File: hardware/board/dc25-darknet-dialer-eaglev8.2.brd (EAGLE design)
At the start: 101.6 x 101.6 mm, 96 parts, among them J1 MF-CON-MICROUSB-RIGHT, SW1 RESET, U1 BU33SD5WG-TR, U2 MCP73831T-5ACI/OT, U3 SOP22FLAT, Y1 CSTCE8M00G52-R0

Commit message: updated schematic to populate audio
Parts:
- C2: value 10uF DNP -> GRM188C80G106ME47D
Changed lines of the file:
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@@
 <attribute name="NAME" x="49.990375" y="32.5755" size="0.6096" layer="26" font="vector" rot="MR180"/>
 </element>
-<element name="C2" library="darknet_parts_library" package="C0603" value="10uF DNP" x="44.846875" y="31.4325" smashed="yes" rot="MR0">
+<element name="C2" library="darknet_parts_library" package="C0603" value="GRM188C80G106ME47D" x="44.846875" y="31.4325" smashed="yes" rot="MR0">
 <attribute name="NAME" x="42.95775" y="31.162625" size="0.6096" layer="26" rot="MR0"/>
 </element>

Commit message: Helps if one saves
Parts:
- R30, R33, R34, R35: value 2K DNP -> 2K
- R31, R32: value 1K DNP -> 1K
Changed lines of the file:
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@@
 </element>
 <element name="U$11" library="darknet_parts_library" package="SPDT_SSAJ120100" value="SWITCH_SPDT" x="50.879375" y="84.93125" rot="MR270"/>
-<element name="R33" library="darknet_parts_library" package="0603-RES" value="2K DNP" x="48.10125" y="35.71875" smashed="yes" rot="MR0">
+<element name="R33" library="darknet_parts_library" package="0603-RES" value="2K" x="48.10125" y="35.71875" smashed="yes" rot="MR0">
 <attribute name="NAME" x="49.990375" y="36.068" size="0.6096" layer="26" font="vector" rot="MR180"/>
 </element>
-<element name="R31" library="darknet_parts_library" package="0603-RES" value="1K DNP" x="44.846875" y="35.71875" smashed="yes" rot="MR180">
+<element name="R31" library="darknet_parts_library" package="0603-RES" value="1K" x="44.846875" y="35.71875" smashed="yes" rot="MR180">
 <attribute name="NAME" x="43.037125" y="35.448875" size="0.6096" layer="26" font="vector" rot="MR0"/>
 </element>
-<element name="R34" library="darknet_parts_library" package="0603-RES" value="2K DNP" x="48.10125" y="33.575625" smashed="yes" rot="MR0">
+<element name="R34" library="darknet_parts_library" package="0603-RES" value="2K" x="48.10125" y="33.575625" smashed="yes" rot="MR0">
 <attribute name="NAME" x="49.990375" y="33.8455" size="0.6096" layer="26" font="vector" rot="MR180"/>
 </element>
-<element name="R32" library="darknet_parts_library" package="0603-RES" value="1K DNP" x="44.846875" y="33.575625" smashed="yes" rot="MR0">
+<element name="R32" library="darknet_parts_library" package="0603-RES" value="1K" x="44.846875" y="33.575625" smashed="yes" rot="MR0">
 <attribute name="NAME" x="43.037125" y="33.226375" size="0.6096" layer="26" font="vector" rot="MR0"/>
 </element>
-<element name="R35" library="darknet_parts_library" package="0603-RES" value="2K DNP" x="48.10125" y="31.4325" smashed="yes" rot="MR0">
+<element name="R35" library="darknet_parts_library" package="0603-RES" value="2K" x="48.10125" y="31.4325" smashed="yes" rot="MR0">
 <attribute name="NAME" x="49.990375" y="32.5755" size="0.6096" layer="26" font="vector" rot="MR180"/>
 </element>
@@
 <attribute name="NAME" x="42.95775" y="31.162625" size="0.6096" layer="26" rot="MR0"/>
 </element>
-<element name="R30" library="darknet_parts_library" package="0603-RES" value="2K DNP" x="44.846875" y="37.861875" smashed="yes" rot="MR0">
+<element name="R30" library="darknet_parts_library" package="0603-RES" value="2K" x="44.846875" y="37.861875" smashed="yes" rot="MR0">
 <attribute name="NAME" x="43.037125" y="37.592" size="0.6096" layer="26" font="vector" rot="MR0"/>
 </element>

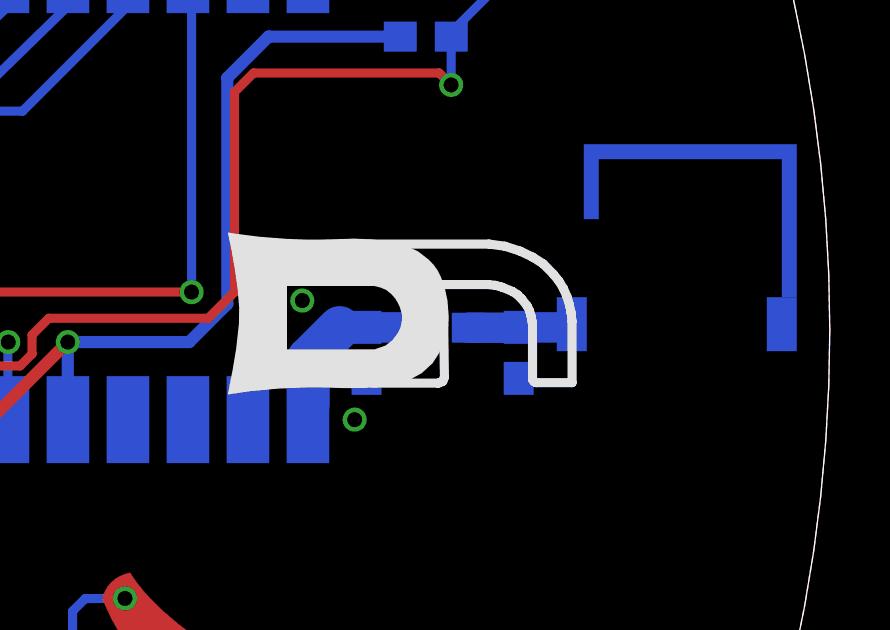
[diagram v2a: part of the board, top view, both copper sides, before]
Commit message: Updated library for new logo
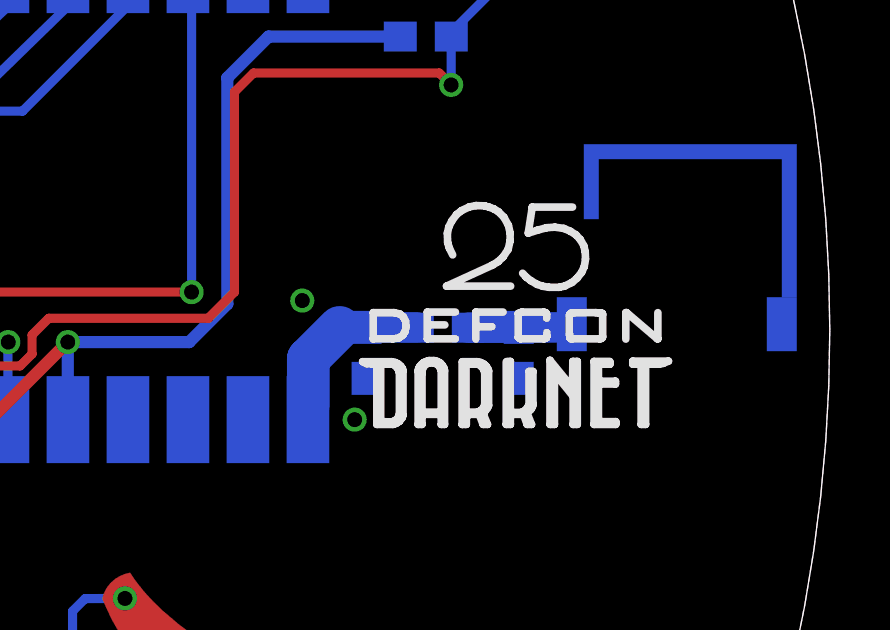
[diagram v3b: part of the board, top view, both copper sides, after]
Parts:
- U$1: value DN_LOGO -> DN_LOGODC25; device SYNShop:DN_LOGO -> SYNShop:DARKNET_LOGO_DC25
- moved U$1 10.3 mm to (91.2, 51.3)
